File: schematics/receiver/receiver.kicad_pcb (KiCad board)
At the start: 4 copper layers, 30.6 x 61.4 mm, 24 parts, among them M1 Servo, M2 Motor, Q1 2N7000, Q2 2N7000, SW1 SW_Nidec_CAS-120A1, U1 PIC16F18324-xSL, U2 LM2937xT, U3 NRF24L01_Breakout, U4 L9110H

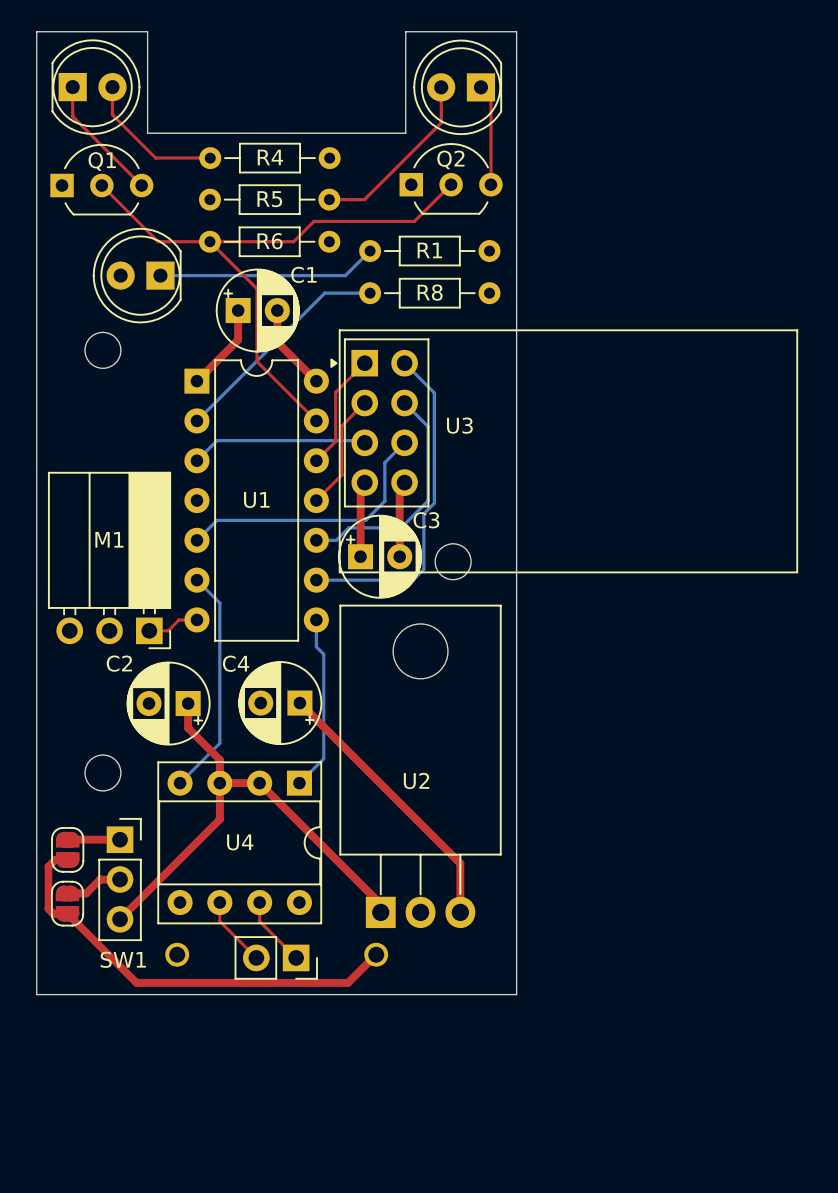
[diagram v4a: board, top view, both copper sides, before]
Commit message: Remove programing ports and reset btn from final boards
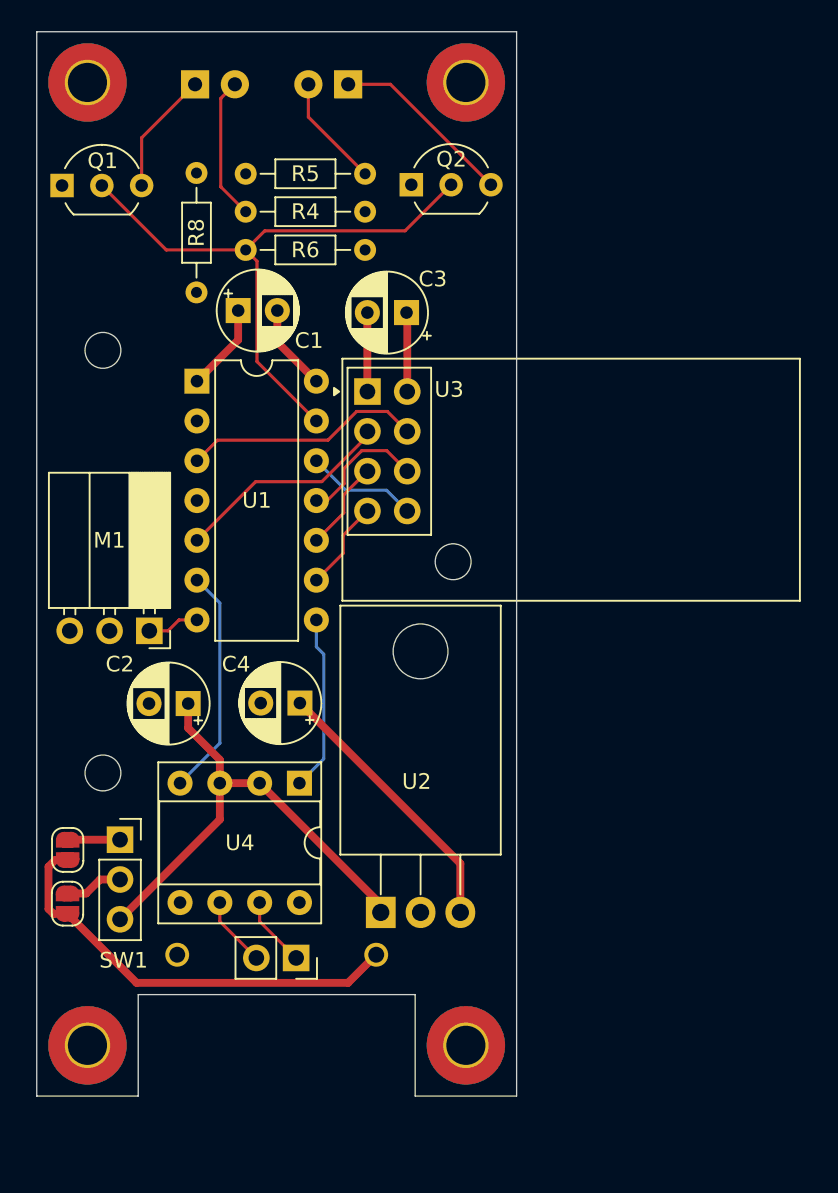
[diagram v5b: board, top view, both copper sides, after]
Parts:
- removed D1: LED, LED_THT:LED_D5.0mm
- removed R1: 470, Resistor_THT:R_Axial_DIN0204_L3.6mm_D1.6mm_P7.62mm_Horizontal
- added H1: MountingHole_Pad, MountingHole:MountingHole_2.5mm_Pad_TopBottom, F.Cu at (121.0, 47.5)
- added H2: MountingHole_Pad, MountingHole:MountingHole_2.5mm_Pad_TopBottom, F.Cu at (121.0, 108.9)
- added H3: MountingHole_Pad, MountingHole:MountingHole_2.5mm_Pad_TopBottom, F.Cu at (145.2, 108.9)
- added H4: MountingHole_Pad, MountingHole:MountingHole_2.5mm_Pad_TopBottom, F.Cu at (145.2, 47.5)
- D2, D3: moved to B.Cu
- moved C3 15.9 mm to (141.4, 62.1), turned to 180 degrees
- moved R8 11.1 mm to (128.0, 60.9), turned to 90 degrees
- moved D3 8.48 mm to (137.7, 47.6)
- moved D2 7.81 mm to (127.9, 47.6)
- moved R4 4.10 mm to (138.7, 55.7)
- moved R5 2.81 mm to (131.1, 53.3)
- moved R6 2.34 mm to (131.1, 58.1)
- moved U3 1.82 mm to (138.9, 67.2)
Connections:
- U1 pad 4: ~{MCLR} -> unconnected-(U1-RA3/~{MCLR}-Pad4)
- U3 pad 1: IRQ -> GND
- U3 pad 2: MISO -> +3.3V
- U3 pad 3: MOSI -> CE
- U3 pad 4: SCK -> CSN
- U3 pad 5: CSN -> SCK
- U3 pad 6: CE -> MOSI
- U3 pad 7: +3.3V -> MISO
- U3 pad 8: GND -> IRQ
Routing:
- net MISO: track 21.4 -> 5.77 mm
- net Net-(U1-RA5): track 14.4 -> 0.00 mm
- net Net-(D1-K): track 14.0 -> 0.00 mm
- net SCK: track 15.0 -> 5.77 mm
- net Net-(D3-K): track 6.48 -> 11.8 mm
- net Net-(D3-A): track 11.4 -> 7.21 mm
- net CSN: track 11.3 -> 15.2 mm
- net CE: track 17.3 -> 13.9 mm
- net LIGHTS: track 39.7 -> 38.7 mm
- net MOSI: track 7.50 -> 8.24 mm
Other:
- board size 30.6 x 61.4 mm -> 30.6 x 67.9 mm

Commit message: Create gerber files and order
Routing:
- net Net-(U1-RA5): track 0.00 -> 9.40 mm
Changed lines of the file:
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@@
 			(outputformat 1)
 			(mirror no)
-			(drillshape 1)
+			(drillshape 0)
 			(scaleselection 1)
-			(outputdirectory "")
+			(outputdirectory "gerber/")
 		)
 	)
@@
 		(net 23)
 	)
+	(segment
+		(start 126.54 62.29)
+		(end 126.54 67.605)
+		(width 0.2)
+		(layer "F.Cu")
+		(net 24)
+	)
+	(segment
+		(start 126.54 67.605)
+		(end 128 69.065)
+		(width 0.2)
+		(layer "F.Cu")
+		(net 24)
+	)
+	(segment
+		(start 127.97 60.86)
+		(end 126.54 62.29)
+		(width 0.2)
+		(layer "F.Cu")
+		(net 24)
+	)
 	(zone

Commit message: Update
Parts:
- removed C4: 10u, Capacitor_THT:CP_Radial_D5.0mm_P2.50mm
- removed JP1, JP2: SolderJumper_2_Open, Jumper:SolderJumper-2_P1.3mm_Open_RoundedPad1.0x1.5mm
- removed U1: PIC16F18324-xSL, Package_DIP:DIP-14_W7.62mm
- removed U2: LM2937xT, Package_TO_SOT_THT:TO-220-3_Horizontal_TabDown
- added BZ1: Buzzer, receiver:XDCR_AT-1224-TWT-5V-2-R, F.Cu at (133.4, 76.9)
- added C10: 22u, Capacitor_Tantalum_SMD:CP_EIA-2012-15_AVX-P, F.Cu at (129.2, 88.0)
- added C5: 0.1u, Capacitor_SMD:C_0402_1005Metric, F.Cu at (124.5, 68.0)
- added C7: 10u, Capacitor_SMD:C_0402_1005Metric, F.Cu at (135.9, 65.9)
- added C9: 10u, Capacitor_SMD:C_0805_2012Metric, F.Cu at (140.8, 85.7)
- added D1: LED, Connector_PinSocket_2.54mm:PinSocket_1x02_P2.54mm_Vertical, F.Cu at (137.6, 46.5)
- added D4: LED, Connector_PinSocket_2.54mm:PinSocket_1x02_P2.54mm_Vertical, F.Cu at (139.6, 114.9)
- added J1: Program, Connector_PinSocket_2.54mm:PinSocket_1x05_P2.54mm_Vertical, F.Cu at (130.1, 52.2)
- added J2: Debug, Connector_PinSocket_2.54mm:PinSocket_1x03_P2.54mm_Vertical, F.Cu at (145.2, 88.9)
- added Q3: 2N7000, Package_TO_SOT_SMD:SOT-23, F.Cu at (121.5, 95.6)
- added Q4: 2N7000, Package_TO_SOT_SMD:SOT-23, F.Cu at (144.3, 95.5)
- added Q5: 2N7000, Package_TO_SOT_SMD:SOT-23, F.Cu at (120.4, 71.3)
- added R1: 10k, Resistor_SMD:R_0402_1005Metric, F.Cu at (126.2, 56.4)
- added R10: 10k, Resistor_SMD:R_0402_1005Metric, F.Cu at (146.0, 100.0)
- added R11: 10k, Resistor_SMD:R_0402_1005Metric, F.Cu at (119.5, 68.0)
- added R12: 470, Resistor_SMD:R_0402_1005Metric, F.Cu at (122.0, 68.0)
- added R2: 470, Resistor_SMD:R_0402_1005Metric, F.Cu at (140.2, 49.8)
- added R3: 1k, Resistor_SMD:R_0402_1005Metric, F.Cu at (126.2, 54.9)
- added R7: 470, Resistor_SMD:R_0402_1005Metric, F.Cu at (143.0, 100.0)
- added R9: 10k, Resistor_SMD:R_0402_1005Metric, F.Cu at (123.0, 100.0)
- added SW2: ~{MCLR}, pcb_radio:SW_1825910-6-4, F.Cu at (121.6, 58.7)
- added U5: PIC32MX170F256B, receiver:SSOP28_MC_MCH, F.Cu at (130.3, 64.4)
- added U6: AMS1117-3.3, Package_TO_SOT_SMD:SOT-223-3_TabPin2, F.Cu at (135.1, 87.1)
- C1, C2: footprint Capacitor_THT:CP_Radial_D5.0mm_P2.50mm -> Capacitor_SMD:C_0402_1005Metric
- C3: footprint Capacitor_THT:CP_Radial_D5.0mm_P2.50mm -> receiver:U2-K_NCH
- D2, D3: footprint LED_THT:LED_D5.0mm -> Connector_PinSocket_2.54mm:PinSocket_1x02_P2.54mm_Vertical; moved to F.Cu
- Q1, Q2: footprint Package_TO_SOT_THT:TO-92_Inline_Wide -> Package_TO_SOT_SMD:SOT-23
- R4, R5, R6, R8: footprint Resistor_THT:R_Axial_DIN0204_L3.6mm_D1.6mm_P7.62mm_Horizontal -> Resistor_SMD:R_0402_1005Metric
- SW1: value SW_Nidec_CAS-120A1 -> Power
- moved D3 64.3 mm to (126.2, 110.9), turned to 90 degrees
- moved R5 48.0 mm to (120.0, 100.0)
- moved C2 29.2 mm to (126.2, 57.9)
- moved SW1 16.4 mm to (139.2, 99.0), turned to 180 degrees
- moved Q1 15.7 mm to (133.9, 48.1), turned to 90 degrees
- moved R8 14.7 mm to (137.5, 49.8), turned to 0 degrees
- moved R4 14.2 mm to (125.9, 49.8), turned to 0 degrees
- moved U3 13.5 mm to (139.3, 53.7)
- moved U4 10.8 mm to (127.2, 100.1), turned to 90 degrees
- moved R6 8.78 mm to (128.5, 49.8)
- moved Q2 7.93 mm to (133.9, 52.3), turned to 90 degrees
- moved M2 7.55 mm to (132.8, 110.7), turned to 90 degrees
- moved M1 5.64 mm to (125.3, 88.1)
- moved C1 5.38 mm to (135.7, 60.2), turned to 90 degrees
- moved C3 5.24 mm to (142.5, 67.3)
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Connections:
- C1 pad 1: +3.3V -> GND
- C1 pad 2: GND -> +3.3V
- C2 pad 1: +9V -> GND
- C2 pad 2: GND -> Net-(C2-Pad2)
- Q1 pad 1: GND -> FL_LIGHTS
- Q1 pad 2: LIGHTS -> GND
- Q2 pad 1: GND -> FR_LIGHTS
- Q2 pad 2: LIGHTS -> GND
- Q2 pad 3: Net-(D3-K) -> Net-(D1-K)
- R6 pad 1: LIGHTS -> GND
- R6 pad 2: GND -> FL_LIGHTS
- R8 pad 1: Net-(U1-RA5) -> GND
- R8 pad 2: GND -> FR_LIGHTS
- SW1 pad 1: Net-(JP2-B) -> unconnected-(SW1-C-Pad1)
- SW1 pad 2: Net-(JP1-B) -> Net-(BT1-+)
- U4 pad 1: PWM5 -> Net-(M2-+)
- U4 pad 4: PWM5.1 -> Net-(M2--)
- U4 pad 6: Net-(M2--) -> PWM4
- U4 pad 7: Net-(M2-+) -> PWM5
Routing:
- net BR_LIGHTS: track 0.00 -> 40.2 mm
- net BL_LIGHTS: track 0.00 -> 39.5 mm
- net LIGHTS: track 38.7 -> 0.00 mm
- net PWM4: track 0.00 -> 29.1 mm, vias 0 -> 1
- net TXD: track 0.00 -> 27.0 mm
- net RXD: track 0.00 -> 25.1 mm
- net PWM6: track 3.33 -> 23.6 mm, vias 0 -> 1
- net Net-(BT1-+): track 27.7 -> 8.05 mm
- net FL_LIGHTS: track 0.00 -> 19.2 mm
- net FR_LIGHTS: track 0.00 -> 18.0 mm
- net Net-(BZ1--): track 0.00 -> 16.3 mm, vias 0 -> 2
- net PWM5: track 11.3 -> 26.0 mm, vias 0 -> 1
- net PWM5.1: track 14.6 -> 0.00 mm
- net Net-(BZ1-+): track 0.00 -> 14.3 mm, vias 0 -> 2
- net PGClk: track 0.00 -> 14.1 mm
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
